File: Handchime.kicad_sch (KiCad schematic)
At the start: 24 parts, among them J1 USB_C_Receptacle_USB2.0_16P, J2 Pins, J3 SWD, SW0 BOOT, SW1 Row 0, Col 0, SW2 Row 0, Col 1, U1 STM32C071GBUx, U2 PRTR5V0U2X, U3 XC6206P332MR-G

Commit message: Fix edge pin alignment and improve silkscreen
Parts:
- J2: PIN10 PB7 -> B7; PIN11 PB8 -> B8; PIN13 PA0 -> A0; PIN14 PA1 -> A1; PIN15 PA2 -> A2; PIN16 PA3 -> A3; PIN17 PA4 -> A4; PIN19 PA5 -> A5; PIN20 PA6 -> A6; PIN21 PA7 -> A7; PIN5 PA15 -> A15; PIN6 PB3 -> B3; PIN7 PB4 -> B4; PIN8 PB5 -> B5; PIN9 PB6 -> B6
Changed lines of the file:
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@@
 			)
 		)
-		(property "PIN5" "PA15"
+		(property "PIN5" "A15"
 			(at 204.47 139.7 0)
 			(hide yes)
@@
 			)
 		)
-		(property "PIN6" "PB3"
+		(property "PIN6" "B3"
 			(at 204.47 139.7 0)
 			(hide yes)
@@
 			)
 		)
-		(property "PIN7" "PB4"
+		(property "PIN7" "B4"
 			(at 204.47 139.7 0)
 			(hide yes)
@@
 			)
 		)
-		(property "PIN8" "PB5"
+		(property "PIN8" "B5"
 			(at 204.47 139.7 0)
 			(hide yes)
@@
 			)
 		)
-		(property "PIN9" "PB6"
+		(property "PIN9" "B6"
 			(at 204.47 139.7 0)
 			(hide yes)
@@
 			)
 		)
-		(property "PIN10" "PB7"
+		(property "PIN10" "B7"
 			(at 204.47 139.7 0)
 			(hide yes)
@@
 			)
 		)
-		(property "PIN11" "PB8"
+		(property "PIN11" "B8"
 			(at 204.47 139.7 0)
 			(hide yes)
@@
 			)
 		)
-		(property "PIN13" "PA0"
+		(property "PIN13" "A0"
 			(at 204.47 139.7 0)
 			(hide yes)
@@
 			)
 		)
-		(property "PIN14" "PA1"
+		(property "PIN14" "A1"
 			(at 204.47 139.7 0)
 			(hide yes)
@@
 			)
 		)
-		(property "PIN15" "PA2"
+		(property "PIN15" "A2"
 			(at 204.47 139.7 0)
 			(hide yes)
@@
 			)
 		)
-		(property "PIN16" "PA3"
+		(property "PIN16" "A3"
 			(at 204.47 139.7 0)
 			(hide yes)
@@
 			)
 		)
-		(property "PIN17" "PA4"
+		(property "PIN17" "A4"
 			(at 204.47 139.7 0)
 			(hide yes)
@@
 			)
 		)
-		(property "PIN19" "PA5"
+		(property "PIN19" "A5"
 			(at 204.47 139.7 0)
 			(hide yes)
@@
 			)
 		)
-		(property "PIN20" "PA6"
+		(property "PIN20" "A6"
 			(at 204.47 139.7 0)
 			(hide yes)
@@
 			)
 		)
-		(property "PIN21" "PA7"
+		(property "PIN21" "A7"
 			(at 204.47 139.7 0)
 			(hide yes)

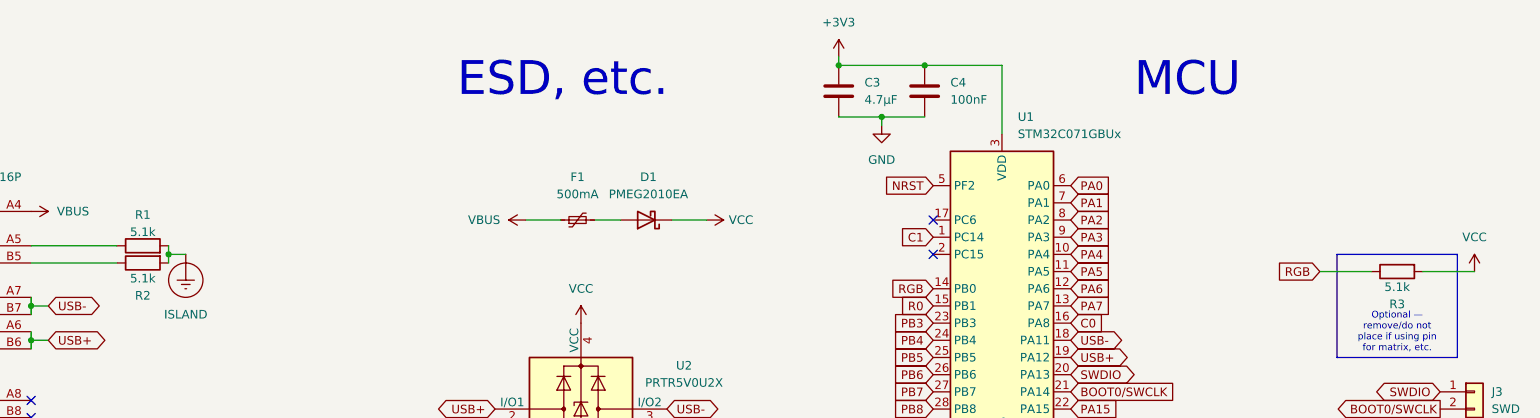
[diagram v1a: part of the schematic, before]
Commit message: Use values instead of references for resistor and capacitor silkscreens
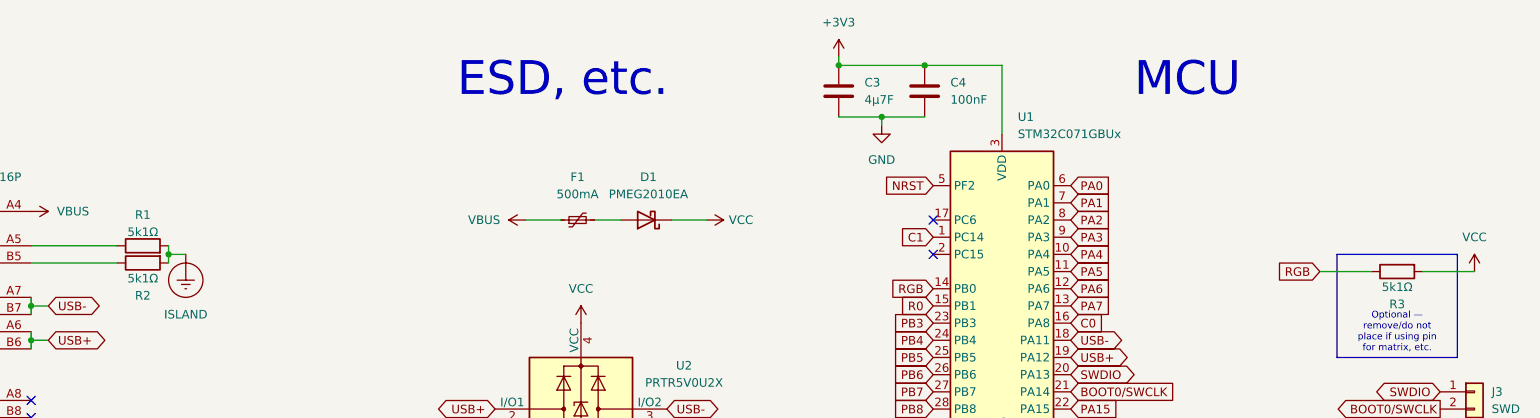
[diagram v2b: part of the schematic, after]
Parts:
- C3: value 4.7µF -> 4µ7F
- R1, R2, R3: value 5.1k -> 5k1Ω
- R4: Label (none) -> 1万Ω
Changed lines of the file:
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@@
 			)
 		)
-		(property "Value" "5.1k"
+		(property "Value" "5k1Ω"
 			(at 62.23 42.418 90)
 			(show_name no)
@@
 			)
 		)
+		(property "Label" "1万Ω"
+			(at 233.68 88.9 90)
+			(hide yes)
+			(show_name no)
+			(do_not_autoplace no)
+			(effects
+				(font
+					(size 1.27 1.27)
+				)
+			)
+		)
 		(pin "1"
 		)
@@
 			)
 		)
-		(property "Value" "5.1k"
+		(property "Value" "5k1Ω"
 			(at 247.65 50.546 90)
 			(show_name no)
@@
 			)
 		)
-		(property "Value" "5.1k"
+		(property "Value" "5k1Ω"
 			(at 62.23 49.276 90)
 			(show_name no)
@@
 			)
 		)
-		(property "Value" "4.7µF"
+		(property "Value" "4µ7F"
 			(at 168.91 22.8599 0)
 			(show_name no)

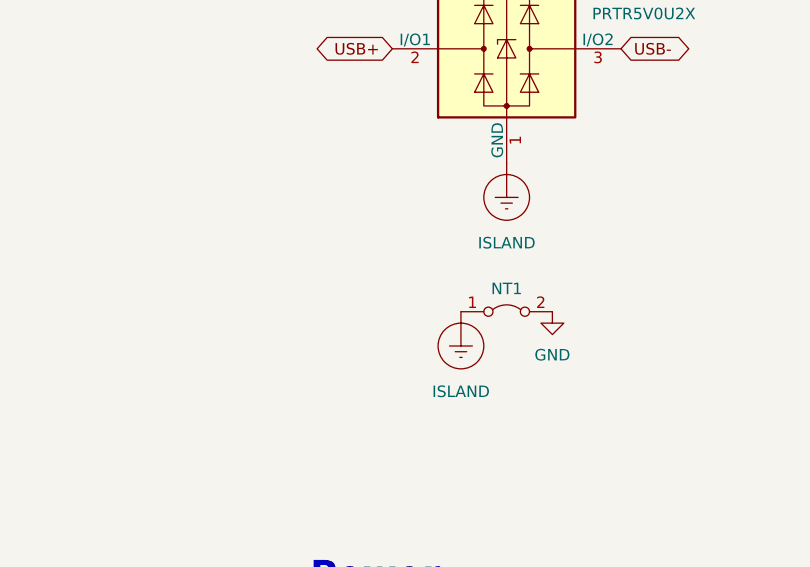
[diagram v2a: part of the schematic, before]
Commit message: Add pad for shield ground connection to (metal) case
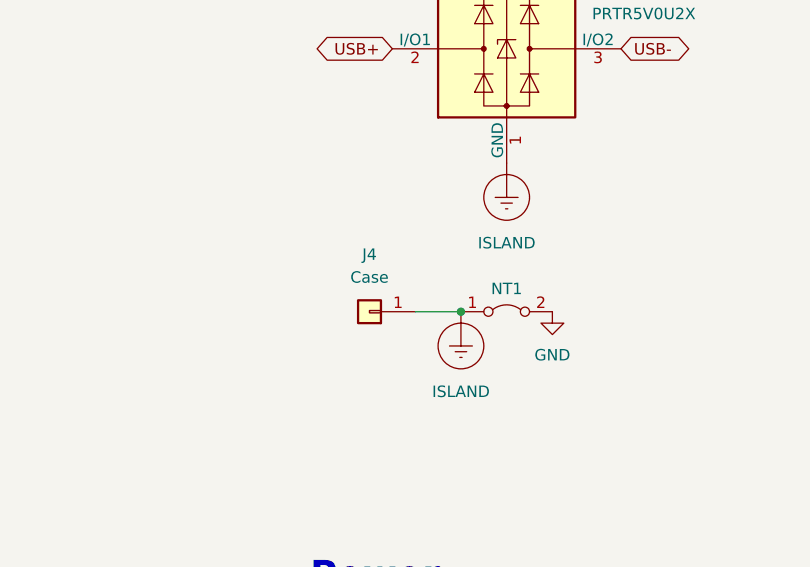
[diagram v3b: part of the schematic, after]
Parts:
- added J4: Case, Project Library:GroundingPoint, symbol Connector_Generic:Conn_01x01
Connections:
- net ISLAND: now also J4.1 (Pin_1)
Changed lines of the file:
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@@
 	)
 	(junction
+		(at 121.92 97.79)
+		(diameter 0)
+		(color 0 0 0 0)
+	)
+	(junction
 		(at 171.45 25.4)
 		(diameter 0)
@@
 	(wire
 		(pts
+			(xy 116.84 97.79) (xy 121.92 97.79)
+		)
+		(stroke
+			(width 0)
+			(type default)
+		)
+	)
+	(wire
+		(pts
 			(xy 45.72 52.07) (xy 45.72 53.34)
 		)
@@
 					(unit 1)
 				)
+			)
+		)
+	)
+	(symbol
+		(lib_id "Connector_Generic:Conn_01x01")
+		(at 111.76 97.79 180)
+		(unit 1)
+		(body_style 1)
+		(exclude_from_sim no)
+		(in_bom yes)
+		(on_board yes)
+		(in_pos_files yes)
+		(dnp no)
+		(fields_autoplaced yes)
+		(property "Reference" "J4"
+			(at 111.76 91.44 0)
+			(show_name no)
+			(do_not_autoplace no)
+			(effects
+				(font
+					(size 1.27 1.27)
+				)
+			)
+		)
+		(property "Value" "Case"
+			(at 111.76 93.98 0)
+			(show_name no)
+			(do_not_autoplace no)
+			(effects
+				(font
+					(size 1.27 1.27)
+				)
+			)
+		)
+		(property "Footprint" "Project Library:GroundingPoint"
+			(at 111.76 97.79 0)
+			(hide yes)
+			(show_name no)
+			(do_not_autoplace no)
+			(effects
+				(font
+					(size 1.27 1.27)
+				)
+			)
+		)
+		(property "Datasheet" ""
+			(at 111.76 97.79 0)
+			(hide yes)
+			(show_name no)
+			(do_not_autoplace no)
+			(effects
+				(font
+					(size 1.27 1.27)
+				)
+			)
+		)
+		(property "Description" "Grounding connection for metal cases"
+			(at 111.76 97.79 0)
+			(hide yes)
+			(show_name no)
+			(do_not_autoplace no)
+			(effects
+				(font
+					(size 1.27 1.27)
+				)
+			)
+		)
+		(pin "1"
+		)
+		(instances
+			(project "Handchime"
+				(path "/34400e51-cf83-464a-b3ec-e9a28a972a27"
+					(reference "J4")
+					(unit 1)
+				)

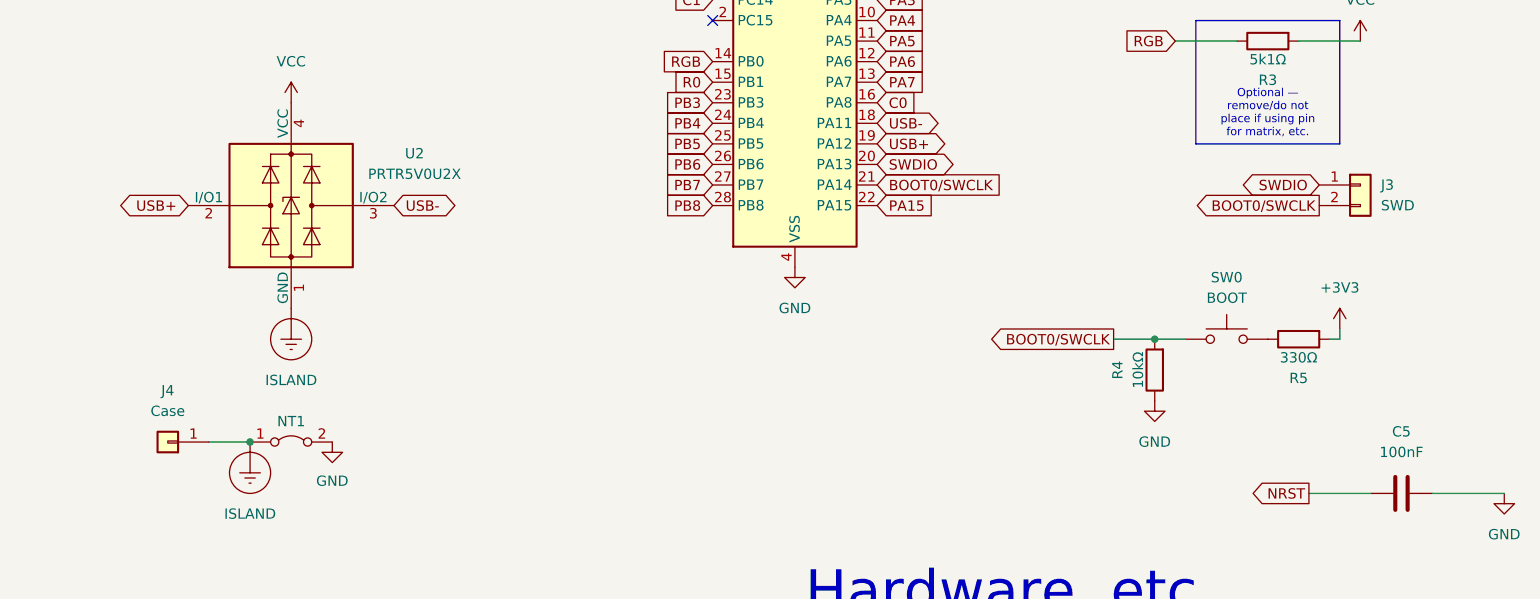
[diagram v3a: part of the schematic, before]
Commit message: Make grounding connection part of SWD access point
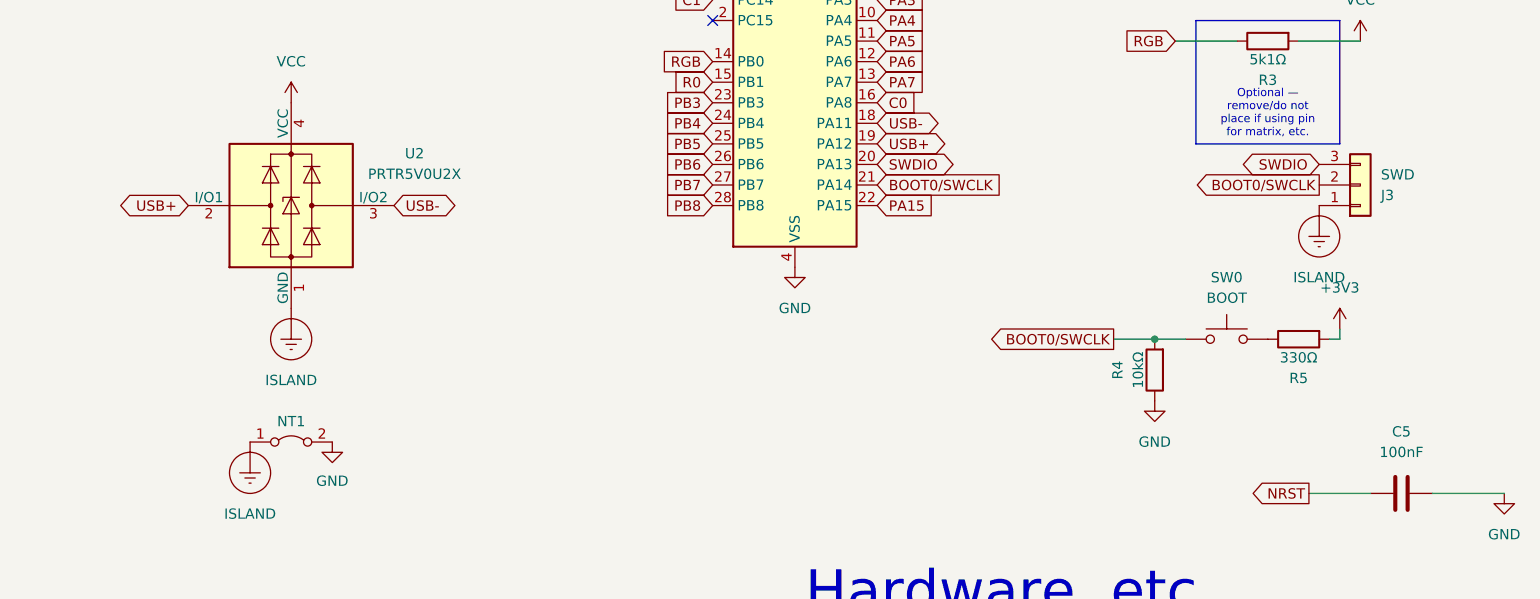
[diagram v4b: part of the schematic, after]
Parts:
- removed J4: Case, Project Library:GroundingPoint, symbol Connector_Generic:Conn_01x01
- J3: footprint Connector_PinHeader_1.00mm:PinHeader_1x02_P1.00mm_Vertical -> Project Library:SWD+GroundingPoint; symbol Connector_Generic:Conn_01x02 -> Connector_Generic:Conn_01x03
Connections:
- net ISLAND: now also J3.1 (Pin_1)
- net SWDIO: now also J3.3 (Pin_3); no longer J3.1 (Pin_1)
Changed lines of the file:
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@@
 	)
 	(junction
-		(at 121.92 97.79)
-		(diameter 0)
-		(color 0 0 0 0)
-	)
-	(junction
 		(at 171.45 25.4)
 		(diameter 0)
@@
 	(wire
 		(pts
-			(xy 116.84 97.79) (xy 121.92 97.79)
-		)
-		(stroke
-			(width 0)
-			(type default)
-		)
-	)
-	(wire
-		(pts
 			(xy 45.72 52.07) (xy 45.72 53.34)
 		)
@@
 	(global_label "SWDIO"
 		(shape bidirectional)
-		(at 254 66.04 180)
+		(at 254 63.5 180)
 		(fields_autoplaced yes)
 		(effects
@@
 		)
 		(property "Intersheetrefs" "${INTERSHEET_REFS}"
-			(at 244.7771 66.04 0)
+			(at 244.7771 63.5 0)
 			(hide yes)
 			(show_name no)
@@
 	(global_label "BOOT0{slash}SWCLK"
 		(shape output)
-		(at 254 68.58 180)
+		(at 254 66.04 180)
 		(fields_autoplaced yes)
 		(effects
@@
 		)
 		(property "Intersheetrefs" "${INTERSHEET_REFS}"
-			(at 239.5047 68.58 0)
+			(at 239.5047 66.04 0)
 			(hide yes)
 			(show_name no)
@@
 	)
 	(symbol
-		(lib_id "Connector_Generic:Conn_01x02")
+		(lib_id "Connector_Generic:Conn_01x03")
 		(at 259.08 66.04 0)
+		(mirror x)
 		(unit 1)
 		(body_style 1)
@@
 		(in_pos_files yes)
 		(dnp no)
-		(fields_autoplaced yes)
 		(property "Reference" "J3"
-			(at 261.62 66.04 0)
+			(at 261.62 67.31 0)
 			(show_name no)
 			(do_not_autoplace no)
@@
 		)
 		(property "Value" "SWD"
-			(at 261.62 68.58 0)
+			(at 261.62 64.77 0)
 			(show_name no)
 			(do_not_autoplace no)
@@
 			)
 		)
-		(property "Footprint" "Connector_PinHeader_1.00mm:PinHeader_1x02_P1.00mm_Vertical"
+		(property "Footprint" "Project Library:SWD+GroundingPoint"
 			(at 259.08 66.04 0)
 			(hide yes)
@@
 			)
 		)
-		(property "Description" "Generic connector, single row, 01x02, script generated (kicad-library-utils/schlib/autogen/connector/)"
+		(property "Description" "Generic connector, single row, 01x03, script generated (kicad-library-utils/schlib/autogen/connector/)"
 			(at 259.08 66.04 0)
 			(hide yes)
@@
 		(pin "2"
 		)
+		(pin "3"
+		)
 		(instances
 			(project "Handchime"
@@
 	)
 	(symbol
-		(lib_id "Connector_Generic:Conn_01x01")
-		(at 111.76 97.79 180)
+		(lib_id "power:VCC")
+		(at 145.542 40.64 270)
 		(unit 1)
 		(body_style 1)
@@
 		(dnp no)
 		(fields_autoplaced yes)
-		(property "Reference" "J4"
-			(at 111.76 91.44 0)
+		(property "Reference" "#PWR03"
+			(at 141.732 40.64 0)
+			(hide yes)
 			(show_name no)
 			(do_not_autoplace no)
@@
 			)
 		)
-		(property "Value" "Case"
-			(at 111.76 93.98 0)
+		(property "Value" "VCC"
+			(at 148.844 40.64 90)
 			(show_name no)
 			(do_not_autoplace no)
@@
 					(size 1.27 1.27)
 				)
+				(justify left)
 			)
 		)
-		(property "Footprint" "Project Library:GroundingPoint"
-			(at 111.76 97.79 0)
+		(property "Footprint" ""
+			(at 145.542 40.64 0)
 			(hide yes)
 			(show_name no)
@@
 		)
 		(property "Datasheet" ""
-			(at 111.76 97.79 0)
+			(at 145.542 40.64 0)
 			(hide yes)
 			(show_name no)
@@
 			)
 		)
-		(property "Description" "Grounding connection for metal cases"
-			(at 111.76 97.79 0)
+		(property "Description" ""
+			(at 145.542 40.64 0)
 			(hide yes)
 			(show_name no)
@@
 			(project "Handchime"
 				(path "/34400e51-cf83-464a-b3ec-e9a28a972a27"
-					(reference "J4")
+					(reference "#PWR03")
 					(unit 1)
 				)
@@
 	)
 	(symbol
-		(lib_id "power:VCC")
-		(at 145.542 40.64 270)
+		(lib_id "power:+5V")
+		(at 201.93 129.54 0)
 		(unit 1)
 		(body_style 1)
@@
 		(in_pos_files yes)
 		(dnp no)
-		(fields_autoplaced yes)
-		(property "Reference" "#PWR03"
-			(at 141.732 40.64 0)
+		(property "Reference" "#PWR010"
+			(at 201.93 133.35 0)
 			(hide yes)
 			(show_name no)
@@
 		)
 		(property "Value" "VCC"
-			(at 148.844 40.64 90)
+			(at 201.9301 125.73 90)
 			(show_name no)
 			(do_not_autoplace no)
@@
 		)
 		(property "Footprint" ""
-			(at 145.542 40.64 0)
+			(at 201.93 129.54 0)
 			(hide yes)
 			(show_name no)
@@
 		)
 		(property "Datasheet" ""
-			(at 145.542 40.64 0)
+			(at 201.93 129.54 0)
 			(hide yes)
 			(show_name no)
@@
 			)
 		)
-		(property "Description" ""
-			(at 145.542 40.64 0)
+		(property "Description" "Power symbol creates a global label with name \"+5V\""
+			(at 201.93 129.54 0)
 			(hide yes)
 			(show_name no)
@@
 			(project "Handchime"
 				(path "/34400e51-cf83-464a-b3ec-e9a28a972a27"
-					(reference "#PWR03")
+					(reference "#PWR010")
 					(unit 1)
 				)
@@
 	)
 	(symbol
-		(lib_id "power:+5V")
-		(at 201.93 129.54 0)
+		(lib_id "power:VBUS")
+		(at 118.872 40.64 90)
 		(unit 1)
 		(body_style 1)
@@
 		(in_pos_files yes)
 		(dnp no)
-		(property "Reference" "#PWR010"
-			(at 201.93 133.35 0)
+		(fields_autoplaced yes)
+		(property "Reference" "#PWR02"
+			(at 122.682 40.64 0)
 			(hide yes)
 			(show_name no)
@@
 			)
 		)
-		(property "Value" "VCC"
-			(at 201.9301 125.73 90)
+		(property "Value" "VBUS"
+			(at 115.062 40.64 90)
 			(show_name no)
 			(do_not_autoplace no)
@@
 		)
 		(property "Footprint" ""
-			(at 201.93 129.54 0)
+			(at 118.872 40.64 0)
 			(hide yes)
 			(show_name no)
@@
 		)
 		(property "Datasheet" ""
-			(at 201.93 129.54 0)
+			(at 118.872 40.64 0)
 			(hide yes)
 			(show_name no)
@@
 			)
 		)
-		(property "Description" "Power symbol creates a global label with name \"+5V\""
-			(at 201.93 129.54 0)
+		(property "Description" ""
+			(at 118.872 40.64 0)
 			(hide yes)
 			(show_name no)
@@
 			(project "Handchime"
 				(path "/34400e51-cf83-464a-b3ec-e9a28a972a27"
-					(reference "#PWR010")
+					(reference "#PWR02")
 					(unit 1)
 				)
@@
 	)
 	(symbol
-		(lib_id "power:VBUS")
-		(at 118.872 40.64 90)
+		(lib_id "power:GND")
+		(at 204.47 149.86 0)
+		(mirror y)
 		(unit 1)
 		(body_style 1)
@@
 		(in_pos_files yes)
 		(dnp no)
-		(fields_autoplaced yes)
-		(property "Reference" "#PWR02"
-			(at 122.682 40.64 0)
+		(property "Reference" "#PWR022"
+			(at 204.47 156.21 0)
 			(hide yes)
 			(show_name no)
@@
 			)
 		)
-		(property "Value" "VBUS"
-			(at 115.062 40.64 90)
+		(property "Value" "GND"
+			(at 204.4701 153.67 90)
 			(show_name no)
 			(do_not_autoplace no)
@@
 					(size 1.27 1.27)
 				)
-				(justify left)
+				(justify right)
 			)
 		)
 		(property "Footprint" ""
-			(at 118.872 40.64 0)
+			(at 204.47 149.86 0)
 			(hide yes)
 			(show_name no)
@@
 		)
 		(property "Datasheet" ""
-			(at 118.872 40.64 0)
+			(at 204.47 149.86 0)
 			(hide yes)
 			(show_name no)
@@
 		)
 		(property "Description" ""
-			(at 118.872 40.64 0)
+			(at 204.47 149.86 0)
 			(hide yes)
 			(show_name no)
@@
 			(project "Handchime"
 				(path "/34400e51-cf83-464a-b3ec-e9a28a972a27"
-					(reference "#PWR02")
+					(reference "#PWR022")
 					(unit 1)
 				)
@@
 	(symbol
 		(lib_id "power:GND")
-		(at 204.47 149.86 0)
-		(mirror y)
+		(at 189.23 76.2 0)
 		(unit 1)
 		(body_style 1)
@@
 		(in_pos_files yes)
 		(dnp no)
-		(property "Reference" "#PWR022"
-			(at 204.47 156.21 0)
+		(fields_autoplaced yes)
+		(property "Reference" "#PWR014"
+			(at 189.23 82.55 0)
 			(hide yes)
 			(show_name no)
@@
 		)
 		(property "Value" "GND"
-			(at 204.4701 153.67 90)
+			(at 189.23 81.28 0)
 			(show_name no)
 			(do_not_autoplace no)
@@
 					(size 1.27 1.27)
 				)
-				(justify right)
 			)
 		)
 		(property "Footprint" ""
-			(at 204.47 149.86 0)
+			(at 189.23 76.2 0)
 			(hide yes)
 			(show_name no)
@@
 		)
 		(property "Datasheet" ""
-			(at 204.47 149.86 0)
+			(at 189.23 76.2 0)
 			(hide yes)
 			(show_name no)
@@
 		)
 		(property "Description" ""
-			(at 204.47 149.86 0)
+			(at 189.23 76.2 0)
 			(hide yes)
 			(show_name no)
@@
 			(project "Handchime"
 				(path "/34400e51-cf83-464a-b3ec-e9a28a972a27"
-					(reference "#PWR022")
+					(reference "#PWR014")
 					(unit 1)
 				)
@@
 	)
 	(symbol
-		(lib_id "power:GND")
-		(at 189.23 76.2 0)
+		(lib_id "power:Earth_Protective")
+		(at 254 68.58 0)
 		(unit 1)
 		(body_style 1)
@@
 		(dnp no)
 		(fields_autoplaced yes)
-		(property "Reference" "#PWR014"
-			(at 189.23 82.55 0)
+		(property "Reference" "#PWR032"
+			(at 254 78.74 0)
 			(hide yes)
 			(show_name no)
@@
 			)
 		)
-		(property "Value" "GND"
-			(at 189.23 81.28 0)
+		(property "Value" "ISLAND"
+			(at 254 77.47 0)
 			(show_name no)
 			(do_not_autoplace no)
@@
 		)
 		(property "Footprint" ""
-			(at 189.23 76.2 0)
+			(at 254 71.12 0)
 			(hide yes)
 			(show_name no)
@@
 		)
 		(property "Datasheet" ""
-			(at 189.23 76.2 0)
+			(at 254 71.12 0)
 			(hide yes)
 			(show_name no)
@@
 			)
 		)
-		(property "Description" ""
-			(at 189.23 76.2 0)
+		(property "Description" "Power symbol creates a global label with name \"Earth_Protective\""
+			(at 254 68.58 0)
 			(hide yes)
 			(show_name no)
@@
 			(project "Handchime"
 				(path "/34400e51-cf83-464a-b3ec-e9a28a972a27"
-					(reference "#PWR014")
+					(reference "#PWR032")
 					(unit 1)
 				)

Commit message: Tweak routing and labelling of CC resistors
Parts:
- R1: Label (none) -> 1
- R2: Label (none) -> 2
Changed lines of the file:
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@@
 			)
 		)
+		(property "Label" "1"
+			(at 62.23 44.45 90)
+			(hide yes)
+			(show_name no)
+			(do_not_autoplace no)
+			(effects
+				(font
+					(size 1.27 1.27)
+				)
+			)
+		)
 		(pin "1"
 		)
@@
 			(at 62.23 46.99 90)
 			(hide yes)
+			(show_name no)
+			(do_not_autoplace no)
+			(effects
+				(font
+					(size 1.27 1.27)
+				)
+			)
+		)
+		(property "Label" "2"
+			(at 62.23 46.99 90)
+			(hide yes)
